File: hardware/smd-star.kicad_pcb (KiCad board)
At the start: 2 copper layers, 50 x 50 mm, 15 parts, among them U1 NE555, U2 4017

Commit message: PCB Routed
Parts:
- removed the D2 at (67.1, 64.6)
- added BT1: BK-883, smd-star:BAT_BK-883, B.Cu at (0.00, 1.02)
- added D10: LED, smd-star:LED_0805_2012Metric_Pad1.15x1.40mm_HandSolder, F.Cu at (7.00, -7.00)
- added D7: LED, smd-star:LED_0805_2012Metric_Pad1.15x1.40mm_HandSolder, F.Cu at (-15.6, -15.6)
- added D9: LED, smd-star:LED_0805_2012Metric_Pad1.15x1.40mm_HandSolder, F.Cu at (-7.00, -7.00)
- moved D6 109.3 mm to (-22.0, 0.00), turned to 0 degrees
- moved D8 108.7 mm to (0.00, -22.0), turned to 270 degrees
- moved R2 105.9 mm to (-6.60, 4.06), turned to 90 degrees
- moved C2 105.7 mm to (-6.60, -0.25), turned to 90 degrees
- moved D1 102.9 mm to (15.6, -15.6), turned to 225 degrees
- moved R1 97.1 mm to (6.60, -0.25), turned to 270 degrees
- moved D5 97.1 mm to (-15.6, 15.6), turned to 45 degrees
- moved R3 94.3 mm to (0.00, 15.5)
- moved C1 92.7 mm to (6.60, 4.06), turned to 270 degrees
- moved U1 92.7 mm to (0.00, -2.29)
- moved D4 85.0 mm to (0.00, 22.0), turned to 90 degrees
- moved D2 84.0 mm to (22.0, 0.00), turned to 180 degrees
- moved U2 83.2 mm to (0.00, 5.00), turned to 90 degrees
- moved D3 75.4 mm to (15.6, 15.6), turned to 135 degrees
- renumbered D8 to D1, D7 to D2, D6 to D3, D5 to D4, D4 to D5, D3 to D6, D1 to D8
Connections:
- D1 pad 2: /LED0 -> /LED1
- D2 pad 2: /LED1 -> /LED2
- D3 pad 2: /LED2 -> /LED3
- D4 pad 2: /LED3 -> /LED4
- D5 pad 2: /LED4 -> /LED5
- D6 pad 2: /LED5 -> /LED6
- D8 pad 2: /LED7 -> /LED8
- U2 pad 1: /LED5 -> /LED6
- U2 pad 10: /LED4 -> /LED5
- U2 pad 11: (no net) -> /LED10
- U2 pad 15: /RESET -> -BATT
- U2 pad 2: /LED1 -> /LED2
- U2 pad 3: /LED0 -> /LED1
- U2 pad 4: /LED2 -> /LED3
- U2 pad 5: /LED6 -> /LED7
- U2 pad 6: /LED7 -> /LED8
- U2 pad 7: /LED3 -> /LED4
- U2 pad 9: /RESET -> /LED9
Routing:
- net /LED8: track 0.00 -> 90.5 mm
- net /LED7: track 0.00 -> 66.3 mm
- net +BATT: track 0.00 -> 54.6 mm, vias 0 -> 2
- net /LED1: track 0.00 -> 53.5 mm
- net -BATT: track 0.00 -> 47.0 mm, vias 0 -> 5
- net /LED_R: track 0.00 -> 35.9 mm, vias 0 -> 13
- net /LED9: track 0.00 -> 32.2 mm
- net /LED2: track 0.00 -> 28.5 mm
- net Net-(R1-Pad2): track 0.00 -> 26.8 mm
- net /LED5: track 0.00 -> 24.8 mm
- net /LED10: track 0.00 -> 20.6 mm
- net /LED3: track 0.00 -> 20.4 mm
- net /LED6: track 0.00 -> 19.6 mm
- net /LED4: track 0.00 -> 15.2 mm
- net Net-(C2-Pad1): track 0.00 -> 13.5 mm
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- added copper zone on B.Cu, net /LED_R
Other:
- rule trace_min: 0.2 -> 0.127

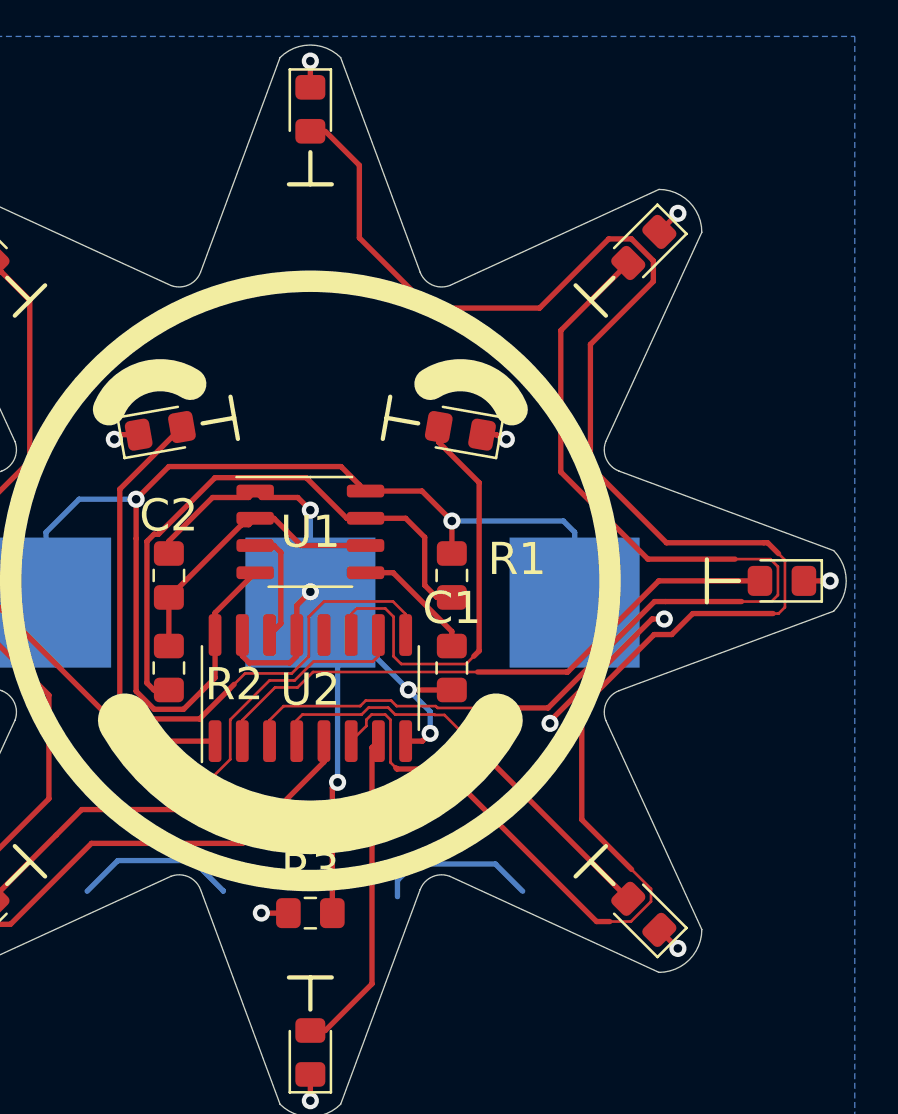
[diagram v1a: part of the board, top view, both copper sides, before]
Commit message: PCB - silk fixes, added missing hanging hole
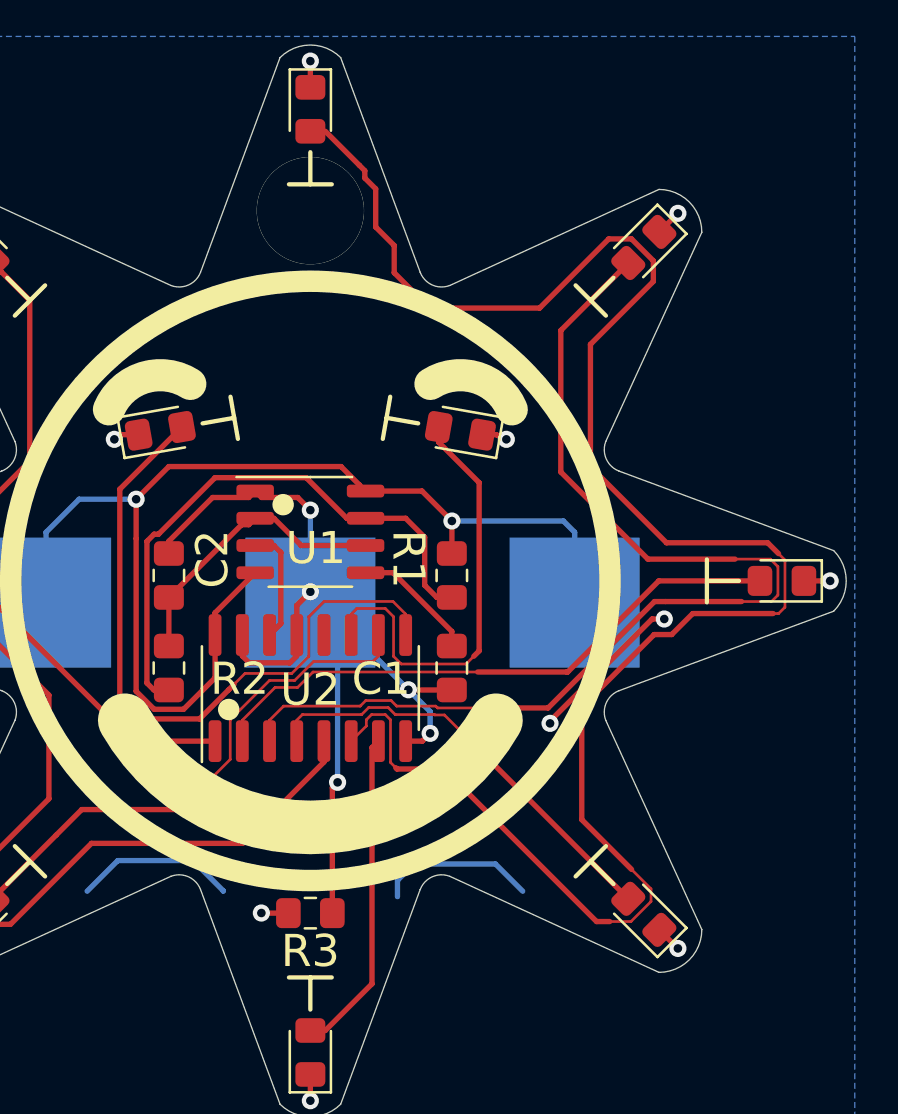
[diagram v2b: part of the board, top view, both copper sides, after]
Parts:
- added G***: LOGO, smd-star:mask_600, B.Cu at (0.25, -8.89)
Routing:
- net /LED_R: vias 13 -> 14
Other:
- board text added: "July2020"
- board text added: "smd-sun.tomk.in"
